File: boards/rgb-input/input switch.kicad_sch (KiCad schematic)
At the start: 5 parts

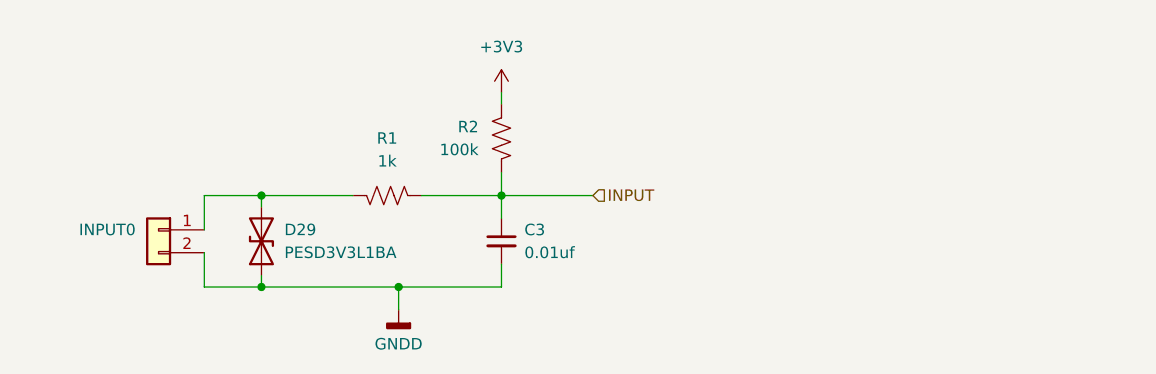
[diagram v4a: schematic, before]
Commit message: more layout checks on the input board
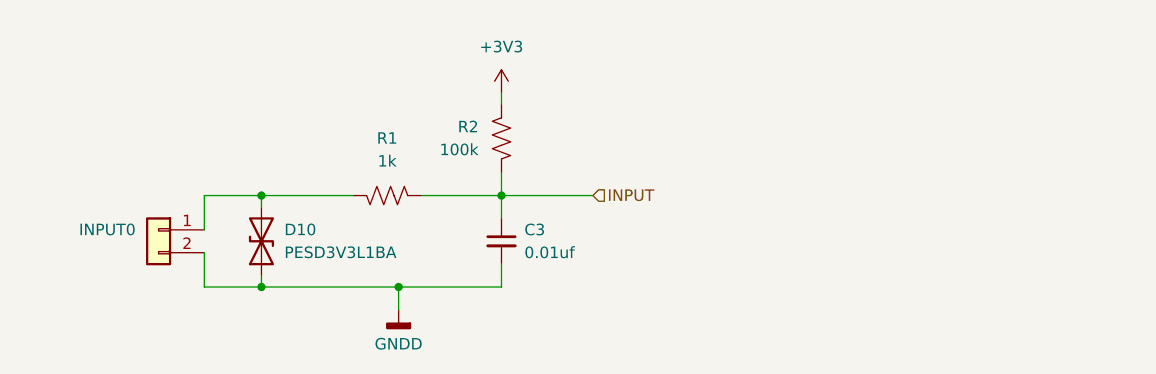
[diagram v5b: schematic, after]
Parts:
- renumbered D29 to D10
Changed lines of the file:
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@@
   (symbol (lib_id "Device:D_TVS") (at 142.24 92.075 90) (unit 1)
     (in_bom yes) (on_board yes) (dnp no)
-    (property "Reference" "D29" (at 144.78 90.805 90)
+    (property "Reference" "D10" (at 144.78 90.805 90)
       (effects (font (size 1.27 1.27)) (justify right))
     )
@@
     (instances
       (project "rgb-input"
+        (path "/c83c6236-96e9-46ad-9d7a-9e2efa4a7966/a581b924-afd8-4b56-b69e-790286072066"
+          (reference "D10") (unit 1)
+        )
+        (path "/c83c6236-96e9-46ad-9d7a-9e2efa4a7966/add74a42-7713-46b0-aac6-4fd9ca032b1b"
+          (reference "D34") (unit 1)
+        )
+        (path "/c83c6236-96e9-46ad-9d7a-9e2efa4a7966/b28a4abb-d7c6-4d37-897c-3a1605d30be6"
+          (reference "D35") (unit 1)
+        )
+        (path "/c83c6236-96e9-46ad-9d7a-9e2efa4a7966/9f4c4100-f7ad-41c6-bb30-0282b2fbed77"
+          (reference "D23") (unit 1)
+        )
+        (path "/c83c6236-96e9-46ad-9d7a-9e2efa4a7966/d9202946-506a-48d9-939c-5d39e3218bd0"
+          (reference "D19") (unit 1)
+        )
+        (path "/c83c6236-96e9-46ad-9d7a-9e2efa4a7966/cf1aab08-94c1-4bc0-914e-a74bb7fd137f"
+          (reference "D20") (unit 1)
+        )
+        (path "/c83c6236-96e9-46ad-9d7a-9e2efa4a7966/2c275ed9-e58a-403d-982f-79a49e483b85"
+          (reference "D21") (unit 1)
+        )
+        (path "/c83c6236-96e9-46ad-9d7a-9e2efa4a7966/9e6cdf4f-246e-427e-8315-a488968192f4"
+          (reference "D22") (unit 1)
+        )
         (path "/c83c6236-96e9-46ad-9d7a-9e2efa4a7966/0036d08f-39b5-4a29-8e4d-ea832b2cc879"
           (reference "D29") (unit 1)
+        )
+        (path "/c83c6236-96e9-46ad-9d7a-9e2efa4a7966/803edf1a-5825-4947-a8b9-85d3a29697e5"
+          (reference "D9") (unit 1)
+        )
+        (path "/c83c6236-96e9-46ad-9d7a-9e2efa4a7966/802175d5-fb4b-4457-a117-b0f397189ff7"
+          (reference "D8") (unit 1)
+        )
+        (path "/c83c6236-96e9-46ad-9d7a-9e2efa4a7966/5fc618b8-7830-4bbf-bf46-7753631e9b1e"
+          (reference "D7") (unit 1)
+        )
+        (path "/c83c6236-96e9-46ad-9d7a-9e2efa4a7966/145fa34f-e19e-43e2-bb48-aff2e824ef0a"
+          (reference "D6") (unit 1)
+        )
+        (path "/c83c6236-96e9-46ad-9d7a-9e2efa4a7966/6f6f2d8d-82f6-4691-bba7-8caa1bd52e96"
+          (reference "D5") (unit 1)
+        )
+        (path "/c83c6236-96e9-46ad-9d7a-9e2efa4a7966/4175a172-5c0b-4d6a-88bb-129f5f07b813"
+          (reference "D4") (unit 1)
+        )
+        (path "/c83c6236-96e9-46ad-9d7a-9e2efa4a7966/4f50afed-9381-4977-8e27-209f0f88ad4e"
+          (reference "D3") (unit 1)
         )
         (path "/c83c6236-96e9-46ad-9d7a-9e2efa4a7966/ef548cdc-9d5d-4f8e-8f54-0c2e96dbe3f0"
           (reference "D2") (unit 1)
         )
-        (path "/c83c6236-96e9-46ad-9d7a-9e2efa4a7966/4f50afed-9381-4977-8e27-209f0f88ad4e"
-          (reference "D3") (unit 1)
-        )
-        (path "/c83c6236-96e9-46ad-9d7a-9e2efa4a7966/4175a172-5c0b-4d6a-88bb-129f5f07b813"
-          (reference "D4") (unit 1)
-        )
-        (path "/c83c6236-96e9-46ad-9d7a-9e2efa4a7966/6f6f2d8d-82f6-4691-bba7-8caa1bd52e96"
-          (reference "D5") (unit 1)
-        )
-        (path "/c83c6236-96e9-46ad-9d7a-9e2efa4a7966/145fa34f-e19e-43e2-bb48-aff2e824ef0a"
-          (reference "D6") (unit 1)
-        )
-        (path "/c83c6236-96e9-46ad-9d7a-9e2efa4a7966/5fc618b8-7830-4bbf-bf46-7753631e9b1e"
-          (reference "D7") (unit 1)
-        )
-        (path "/c83c6236-96e9-46ad-9d7a-9e2efa4a7966/802175d5-fb4b-4457-a117-b0f397189ff7"
-          (reference "D8") (unit 1)
-        )
-        (path "/c83c6236-96e9-46ad-9d7a-9e2efa4a7966/803edf1a-5825-4947-a8b9-85d3a29697e5"
-          (reference "D9") (unit 1)
-        )
-        (path "/c83c6236-96e9-46ad-9d7a-9e2efa4a7966/a581b924-afd8-4b56-b69e-790286072066"
-          (reference "D10") (unit 1)
-        )
-        (path "/c83c6236-96e9-46ad-9d7a-9e2efa4a7966/9e6cdf4f-246e-427e-8315-a488968192f4"
-          (reference "D22") (unit 1)
-        )
-        (path "/c83c6236-96e9-46ad-9d7a-9e2efa4a7966/2c275ed9-e58a-403d-982f-79a49e483b85"
-          (reference "D21") (unit 1)
-        )
-        (path "/c83c6236-96e9-46ad-9d7a-9e2efa4a7966/cf1aab08-94c1-4bc0-914e-a74bb7fd137f"
-          (reference "D20") (unit 1)
-        )
-        (path "/c83c6236-96e9-46ad-9d7a-9e2efa4a7966/d9202946-506a-48d9-939c-5d39e3218bd0"
-          (reference "D19") (unit 1)
-        )
-        (path "/c83c6236-96e9-46ad-9d7a-9e2efa4a7966/9f4c4100-f7ad-41c6-bb30-0282b2fbed77"
-          (reference "D23") (unit 1)
-        )
-        (path "/c83c6236-96e9-46ad-9d7a-9e2efa4a7966/b28a4abb-d7c6-4d37-897c-3a1605d30be6"
-          (reference "D35") (unit 1)
-        )
-        (path "/c83c6236-96e9-46ad-9d7a-9e2efa4a7966/add74a42-7713-46b0-aac6-4fd9ca032b1b"
-          (reference "D34") (unit 1)
-        )
       )

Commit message: routed the rgb setup
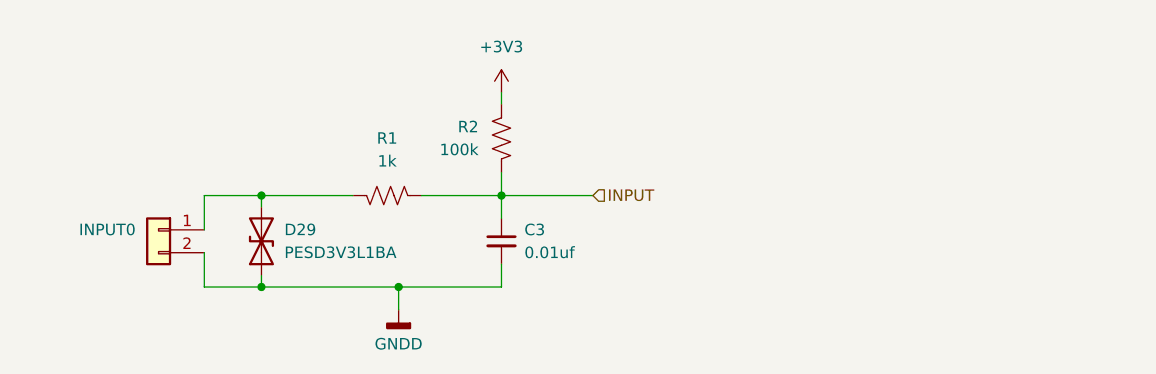
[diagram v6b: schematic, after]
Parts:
- renumbered D10 to D29
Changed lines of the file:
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@@
   (symbol (lib_id "Device:D_TVS") (at 142.24 92.075 90) (unit 1)
     (in_bom yes) (on_board yes) (dnp no)
-    (property "Reference" "D10" (at 144.78 90.805 90)
+    (property "Reference" "D29" (at 144.78 90.805 90)
       (effects (font (size 1.27 1.27)) (justify right))
     )
@@
     (instances
       (project "rgb-input"
-        (path "/c83c6236-96e9-46ad-9d7a-9e2efa4a7966/a581b924-afd8-4b56-b69e-790286072066"
-          (reference "D10") (unit 1)
+        (path "/c83c6236-96e9-46ad-9d7a-9e2efa4a7966/0036d08f-39b5-4a29-8e4d-ea832b2cc879"
+          (reference "D29") (unit 1)
         )
         (path "/c83c6236-96e9-46ad-9d7a-9e2efa4a7966/add74a42-7713-46b0-aac6-4fd9ca032b1b"
@@
           (reference "D22") (unit 1)
         )
-        (path "/c83c6236-96e9-46ad-9d7a-9e2efa4a7966/0036d08f-39b5-4a29-8e4d-ea832b2cc879"
-          (reference "D29") (unit 1)
-        )
         (path "/c83c6236-96e9-46ad-9d7a-9e2efa4a7966/803edf1a-5825-4947-a8b9-85d3a29697e5"
           (reference "D9") (unit 1)
         )
+        (path "/c83c6236-96e9-46ad-9d7a-9e2efa4a7966/a581b924-afd8-4b56-b69e-790286072066"
+          (reference "D10") (unit 1)
+        )
         (path "/c83c6236-96e9-46ad-9d7a-9e2efa4a7966/802175d5-fb4b-4457-a117-b0f397189ff7"

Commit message: so much routing.
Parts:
- renumbered D29 to D9
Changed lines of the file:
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@@
   (symbol (lib_id "Device:D_TVS") (at 142.24 92.075 90) (unit 1)
     (in_bom yes) (on_board yes) (dnp no)
-    (property "Reference" "D29" (at 144.78 90.805 90)
+    (property "Reference" "D9" (at 144.78 90.805 90)
       (effects (font (size 1.27 1.27)) (justify right))
     )
@@
     (instances
       (project "rgb-input"
+        (path "/c83c6236-96e9-46ad-9d7a-9e2efa4a7966/803edf1a-5825-4947-a8b9-85d3a29697e5"
+          (reference "D9") (unit 1)
+        )
+        (path "/c83c6236-96e9-46ad-9d7a-9e2efa4a7966/ef548cdc-9d5d-4f8e-8f54-0c2e96dbe3f0"
+          (reference "D2") (unit 1)
+        )
+        (path "/c83c6236-96e9-46ad-9d7a-9e2efa4a7966/4f50afed-9381-4977-8e27-209f0f88ad4e"
+          (reference "D3") (unit 1)
+        )
+        (path "/c83c6236-96e9-46ad-9d7a-9e2efa4a7966/4175a172-5c0b-4d6a-88bb-129f5f07b813"
+          (reference "D4") (unit 1)
+        )
+        (path "/c83c6236-96e9-46ad-9d7a-9e2efa4a7966/6f6f2d8d-82f6-4691-bba7-8caa1bd52e96"
+          (reference "D5") (unit 1)
+        )
+        (path "/c83c6236-96e9-46ad-9d7a-9e2efa4a7966/145fa34f-e19e-43e2-bb48-aff2e824ef0a"
+          (reference "D6") (unit 1)
+        )
+        (path "/c83c6236-96e9-46ad-9d7a-9e2efa4a7966/5fc618b8-7830-4bbf-bf46-7753631e9b1e"
+          (reference "D7") (unit 1)
+        )
+        (path "/c83c6236-96e9-46ad-9d7a-9e2efa4a7966/802175d5-fb4b-4457-a117-b0f397189ff7"
+          (reference "D8") (unit 1)
+        )
+        (path "/c83c6236-96e9-46ad-9d7a-9e2efa4a7966/a581b924-afd8-4b56-b69e-790286072066"
+          (reference "D10") (unit 1)
+        )
         (path "/c83c6236-96e9-46ad-9d7a-9e2efa4a7966/0036d08f-39b5-4a29-8e4d-ea832b2cc879"
           (reference "D29") (unit 1)
+        )
+        (path "/c83c6236-96e9-46ad-9d7a-9e2efa4a7966/9e6cdf4f-246e-427e-8315-a488968192f4"
+          (reference "D22") (unit 1)
+        )
+        (path "/c83c6236-96e9-46ad-9d7a-9e2efa4a7966/2c275ed9-e58a-403d-982f-79a49e483b85"
+          (reference "D21") (unit 1)
+        )
+        (path "/c83c6236-96e9-46ad-9d7a-9e2efa4a7966/cf1aab08-94c1-4bc0-914e-a74bb7fd137f"
+          (reference "D20") (unit 1)
+        )
+        (path "/c83c6236-96e9-46ad-9d7a-9e2efa4a7966/d9202946-506a-48d9-939c-5d39e3218bd0"
+          (reference "D19") (unit 1)
+        )
+        (path "/c83c6236-96e9-46ad-9d7a-9e2efa4a7966/9f4c4100-f7ad-41c6-bb30-0282b2fbed77"
+          (reference "D23") (unit 1)
+        )
+        (path "/c83c6236-96e9-46ad-9d7a-9e2efa4a7966/b28a4abb-d7c6-4d37-897c-3a1605d30be6"
+          (reference "D35") (unit 1)
         )
         (path "/c83c6236-96e9-46ad-9d7a-9e2efa4a7966/add74a42-7713-46b0-aac6-4fd9ca032b1b"
           (reference "D34") (unit 1)
         )
-        (path "/c83c6236-96e9-46ad-9d7a-9e2efa4a7966/b28a4abb-d7c6-4d37-897c-3a1605d30be6"
-          (reference "D35") (unit 1)
-        )
-        (path "/c83c6236-96e9-46ad-9d7a-9e2efa4a7966/9f4c4100-f7ad-41c6-bb30-0282b2fbed77"
-          (reference "D23") (unit 1)
-        )
-        (path "/c83c6236-96e9-46ad-9d7a-9e2efa4a7966/d9202946-506a-48d9-939c-5d39e3218bd0"
-          (reference "D19") (unit 1)
-        )
-        (path "/c83c6236-96e9-46ad-9d7a-9e2efa4a7966/cf1aab08-94c1-4bc0-914e-a74bb7fd137f"
-          (reference "D20") (unit 1)
-        )
-        (path "/c83c6236-96e9-46ad-9d7a-9e2efa4a7966/2c275ed9-e58a-403d-982f-79a49e483b85"
-          (reference "D21") (unit 1)
-        )
-        (path "/c83c6236-96e9-46ad-9d7a-9e2efa4a7966/9e6cdf4f-246e-427e-8315-a488968192f4"
-          (reference "D22") (unit 1)
-        )
-        (path "/c83c6236-96e9-46ad-9d7a-9e2efa4a7966/803edf1a-5825-4947-a8b9-85d3a29697e5"
-          (reference "D9") (unit 1)
-        )
-        (path "/c83c6236-96e9-46ad-9d7a-9e2efa4a7966/a581b924-afd8-4b56-b69e-790286072066"
-          (reference "D10") (unit 1)
-        )
-        (path "/c83c6236-96e9-46ad-9d7a-9e2efa4a7966/802175d5-fb4b-4457-a117-b0f397189ff7"
-          (reference "D8") (unit 1)
-        )
-        (path "/c83c6236-96e9-46ad-9d7a-9e2efa4a7966/5fc618b8-7830-4bbf-bf46-7753631e9b1e"
-          (reference "D7") (unit 1)
-        )
-        (path "/c83c6236-96e9-46ad-9d7a-9e2efa4a7966/145fa34f-e19e-43e2-bb48-aff2e824ef0a"
-          (reference "D6") (unit 1)
-        )
-        (path "/c83c6236-96e9-46ad-9d7a-9e2efa4a7966/6f6f2d8d-82f6-4691-bba7-8caa1bd52e96"
-          (reference "D5") (unit 1)
-        )
-        (path "/c83c6236-96e9-46ad-9d7a-9e2efa4a7966/4175a172-5c0b-4d6a-88bb-129f5f07b813"
-          (reference "D4") (unit 1)
-        )
-        (path "/c83c6236-96e9-46ad-9d7a-9e2efa4a7966/4f50afed-9381-4977-8e27-209f0f88ad4e"
-          (reference "D3") (unit 1)
-        )
-        (path "/c83c6236-96e9-46ad-9d7a-9e2efa4a7966/ef548cdc-9d5d-4f8e-8f54-0c2e96dbe3f0"
-          (reference "D2") (unit 1)
-        )
       )

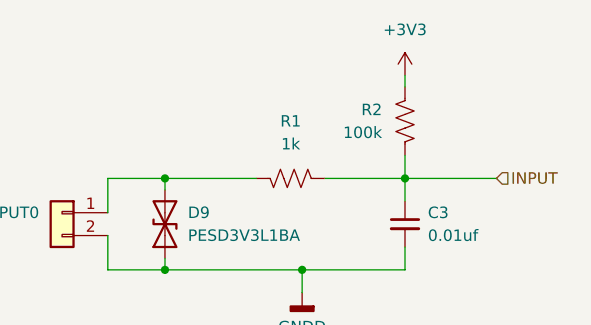
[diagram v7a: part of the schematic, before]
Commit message: whoa, board is fully routed!!!!
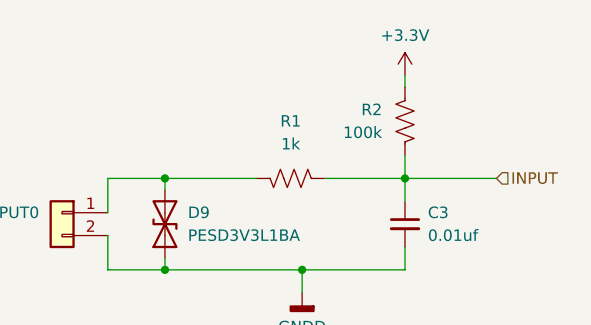
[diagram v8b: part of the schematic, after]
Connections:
- net +3V3 renamed +3.3V
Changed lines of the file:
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@@
-    )
-  )
-  (symbol (lib_id "power:+3V3") (at 168.91 75.565 0) (mirror y) (unit 1)
-    (in_bom yes) (on_board yes) (dnp no) (fields_autoplaced)
-    (property "Reference" "#PWR01" (at 168.91 79.375 0)
-      (effects (font (size 1.27 1.27)) hide)
-    )
-    (property "Value" "+3V3" (at 168.91 70.485 0)
-      (effects (font (size 1.27 1.27)))
-    )
-    (property "Footprint" "" (at 168.91 75.565 0)
-      (effects (font (size 1.27 1.27)) hide)
-    )
-    (property "Datasheet" "" (at 168.91 75.565 0)
-      (effects (font (size 1.27 1.27)) hide)
-    )
-    (pin "1")
-    (instances
-      (project "rgb-input"
-        (path "/c83c6236-96e9-46ad-9d7a-9e2efa4a7966/ef548cdc-9d5d-4f8e-8f54-0c2e96dbe3f0"
-          (reference "#PWR01") (unit 1)
-        )
-        (path "/c83c6236-96e9-46ad-9d7a-9e2efa4a7966/4f50afed-9381-4977-8e27-209f0f88ad4e"
-          (reference "#PWR012") (unit 1)
-        )
-        (path "/c83c6236-96e9-46ad-9d7a-9e2efa4a7966/4175a172-5c0b-4d6a-88bb-129f5f07b813"
-          (reference "#PWR014") (unit 1)
-        )
-        (path "/c83c6236-96e9-46ad-9d7a-9e2efa4a7966/6f6f2d8d-82f6-4691-bba7-8caa1bd52e96"
-          (reference "#PWR016") (unit 1)
-        )
-        (path "/c83c6236-96e9-46ad-9d7a-9e2efa4a7966/145fa34f-e19e-43e2-bb48-aff2e824ef0a"
-          (reference "#PWR018") (unit 1)
-        )
-        (path "/c83c6236-96e9-46ad-9d7a-9e2efa4a7966/5fc618b8-7830-4bbf-bf46-7753631e9b1e"
-          (reference "#PWR020") (unit 1)
-        )
-        (path "/c83c6236-96e9-46ad-9d7a-9e2efa4a7966/802175d5-fb4b-4457-a117-b0f397189ff7"
-          (reference "#PWR022") (unit 1)
-        )
-        (path "/c83c6236-96e9-46ad-9d7a-9e2efa4a7966/803edf1a-5825-4947-a8b9-85d3a29697e5"
-          (reference "#PWR024") (unit 1)
-        )
-        (path "/c83c6236-96e9-46ad-9d7a-9e2efa4a7966/a581b924-afd8-4b56-b69e-790286072066"
-          (reference "#PWR026") (unit 1)
-        )
-        (path "/c83c6236-96e9-46ad-9d7a-9e2efa4a7966/9e6cdf4f-246e-427e-8315-a488968192f4"
-          (reference "#PWR051") (unit 1)
-        )
-        (path "/c83c6236-96e9-46ad-9d7a-9e2efa4a7966/2c275ed9-e58a-403d-982f-79a49e483b85"
-          (reference "#PWR049") (unit 1)
-        )
-        (path "/c83c6236-96e9-46ad-9d7a-9e2efa4a7966/cf1aab08-94c1-4bc0-914e-a74bb7fd137f"
-          (reference "#PWR047") (unit 1)
-        )
-        (path "/c83c6236-96e9-46ad-9d7a-9e2efa4a7966/d9202946-506a-48d9-939c-5d39e3218bd0"
-          (reference "#PWR045") (unit 1)
-        )
-        (path "/c83c6236-96e9-46ad-9d7a-9e2efa4a7966/9f4c4100-f7ad-41c6-bb30-0282b2fbed77"
-          (reference "#PWR053") (unit 1)
-        )
-        (path "/c83c6236-96e9-46ad-9d7a-9e2efa4a7966/b28a4abb-d7c6-4d37-897c-3a1605d30be6"
-          (reference "#PWR068") (unit 1)
-        )
-        (path "/c83c6236-96e9-46ad-9d7a-9e2efa4a7966/add74a42-7713-46b0-aac6-4fd9ca032b1b"
-          (reference "#PWR066") (unit 1)
-        )
-      )
     )
   )
@@
         )
       )
+    )
+  )
+  (symbol (lib_id "power:+3.3V") (at 168.91 75.565 0) (unit 1)
+    (in_bom yes) (on_board yes) (dnp no) (fields_autoplaced)
+    (property "Reference" "#PWR01" (at 168.91 79.375 0)
+      (effects (font (size 1.27 1.27)) hide)
+    )
+    (property "Value" "+3.3V" (at 168.91 71.12 0)
+      (effects (font (size 1.27 1.27)))
+    )
+    (property "Footprint" "" (at 168.91 75.565 0)
+      (effects (font (size 1.27 1.27)) hide)
+    )
+    (property "Datasheet" "" (at 168.91 75.565 0)
+      (effects (font (size 1.27 1.27)) hide)
+    )
+    (pin "1")
+    (instances
+      (project "rgb-input"
+        (path "/c83c6236-96e9-46ad-9d7a-9e2efa4a7966/4f50afed-9381-4977-8e27-209f0f88ad4e"
+          (reference "#PWR01") (unit 1)
+        )
+        (path "/c83c6236-96e9-46ad-9d7a-9e2efa4a7966/6f6f2d8d-82f6-4691-bba7-8caa1bd52e96"
+          (reference "#PWR09") (unit 1)
+        )
+        (path "/c83c6236-96e9-46ad-9d7a-9e2efa4a7966/4175a172-5c0b-4d6a-88bb-129f5f07b813"
+          (reference "#PWR010") (unit 1)
+        )
+        (path "/c83c6236-96e9-46ad-9d7a-9e2efa4a7966/ef548cdc-9d5d-4f8e-8f54-0c2e96dbe3f0"
+          (reference "#PWR012") (unit 1)
+        )
+        (path "/c83c6236-96e9-46ad-9d7a-9e2efa4a7966/145fa34f-e19e-43e2-bb48-aff2e824ef0a"
+          (reference "#PWR014") (unit 1)
+        )
+        (path "/c83c6236-96e9-46ad-9d7a-9e2efa4a7966/5fc618b8-7830-4bbf-bf46-7753631e9b1e"
+          (reference "#PWR016") (unit 1)
+        )
+        (path "/c83c6236-96e9-46ad-9d7a-9e2efa4a7966/802175d5-fb4b-4457-a117-b0f397189ff7"
+          (reference "#PWR018") (unit 1)
+        )
+        (path "/c83c6236-96e9-46ad-9d7a-9e2efa4a7966/803edf1a-5825-4947-a8b9-85d3a29697e5"
+          (reference "#PWR020") (unit 1)
+        )
+        (path "/c83c6236-96e9-46ad-9d7a-9e2efa4a7966/a581b924-afd8-4b56-b69e-790286072066"
+          (reference "#PWR022") (unit 1)
+        )
+        (path "/c83c6236-96e9-46ad-9d7a-9e2efa4a7966/d9202946-506a-48d9-939c-5d39e3218bd0"
+          (reference "#PWR024") (unit 1)
+        )
+        (path "/c83c6236-96e9-46ad-9d7a-9e2efa4a7966/cf1aab08-94c1-4bc0-914e-a74bb7fd137f"
+          (reference "#PWR026") (unit 1)
+        )
+        (path "/c83c6236-96e9-46ad-9d7a-9e2efa4a7966/2c275ed9-e58a-403d-982f-79a49e483b85"
+          (reference "#PWR045") (unit 1)
+        )
+        (path "/c83c6236-96e9-46ad-9d7a-9e2efa4a7966/9e6cdf4f-246e-427e-8315-a488968192f4"
+          (reference "#PWR047") (unit 1)
+        )
+        (path "/c83c6236-96e9-46ad-9d7a-9e2efa4a7966/9f4c4100-f7ad-41c6-bb30-0282b2fbed77"
+          (reference "#PWR049") (unit 1)
+        )
+        (path "/c83c6236-96e9-46ad-9d7a-9e2efa4a7966/add74a42-7713-46b0-aac6-4fd9ca032b1b"
+          (reference "#PWR051") (unit 1)
+        )
+        (path "/c83c6236-96e9-46ad-9d7a-9e2efa4a7966/b28a4abb-d7c6-4d37-897c-3a1605d30be6"
+          (reference "#PWR053") (unit 1)
+        )
+      )
